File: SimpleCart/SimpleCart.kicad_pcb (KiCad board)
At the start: 2 copper layers, 90 x 56.8 mm, 9 parts, among them J1 CommanderX16Expansion Alt, U1 SST39SF040, U2 74HCT00, U3 74HCT138

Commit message: BOM, fully routed
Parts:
- C1, C2, C3: value C -> 100nF; footprint Capacitor_THT:C_Disc_D5.0mm_W2.5mm_P5.00mm -> Capacitor_THT:C_Axial_L3.8mm_D2.6mm_P7.50mm_Horizontal
- JP1: value Jumper_2_Bridged -> WRITE EN
- U1: value SST39SF040 -> SST39SF040 (ROM)
- moved C1 50.8 mm to (134.0, 115.5), turned to 90 degrees
- moved U1 28.8 mm to (129.1, 121.2), turned to 90 degrees
- moved U3 27.8 mm to (74.0, 121.5)
- moved JP1 26.5 mm to (108.2, 102.7), turned to 0 degrees
- moved C3 24.9 mm to (62.5, 109.9)
- moved U2 18.6 mm to (66.5, 102.2), turned to -90 degrees
- moved C2 12.7 mm to (77.7, 113.4), turned to -90 degrees
- moved R1 12.0 mm to (116.2, 102.7), turned to 0 degrees
- moved J1 0.60 mm to (93.0, 130.8)
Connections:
- net Net-(J1-A0) renamed A0
- net Net-(J1-A1) renamed A1
- net Net-(J1-A10) renamed A10
- net Net-(J1-A11) renamed A11
- net Net-(J1-A12) renamed A12
- net Net-(J1-A13) renamed A13
- net Net-(J1-A2) renamed A2
- net Net-(J1-A3) renamed A3
- net Net-(J1-A4) renamed A4
- net Net-(J1-A5) renamed A5
- net Net-(J1-A6) renamed A6
- net Net-(J1-A7) renamed A7
- net Net-(J1-A8) renamed A8
- net Net-(J1-A9) renamed A9
- net Net-(J1-D0) renamed D0
- net Net-(J1-D1) renamed D1
- net Net-(J1-D2) renamed D2
- net Net-(J1-D3) renamed D3
- net Net-(J1-D4) renamed D4
- net Net-(J1-D5) renamed D5
- net Net-(J1-D6) renamed D6
- net Net-(J1-D7) renamed D7
- net Net-(J1-ROMB0) renamed ROMB0
- net Net-(J1-ROMB1) renamed ROMB1
- net Net-(J1-ROMB2) renamed ROMB2
- net Net-(J1-ROMB3) renamed ROMB3
- net Net-(J1-ROMB4) renamed ROMB4
- U3 pad 14: unconnected-(U3-~{Y1}-Pad14) -> !RAMBEN
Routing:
- net +5V: track 0.00 -> 99.0 mm
- net GND: track 0.00 -> 96.6 mm
- net ROMB0: track 0.00 -> 73.8 mm, vias 0 -> 1
- net Net-(J1-A14): track 0.00 -> 67.6 mm, vias 0 -> 3
- net ROMB3: track 0.00 -> 65.9 mm, vias 0 -> 1
- net ROMB1: track 0.00 -> 64.6 mm
- net ROMB2: track 0.00 -> 64.4 mm
- net ROMB4: track 0.00 -> 63.7 mm, vias 0 -> 2
- net Net-(J1-A15): track 0.00 -> 60.2 mm, vias 0 -> 3
- net !ROMBEN: track 0.00 -> 41.7 mm
- net A10: track 0.00 -> 39.0 mm, vias 0 -> 1
- net Net-(J1-RWB): track 0.00 -> 38.4 mm, vias 0 -> 2
- net A11: track 0.00 -> 37.9 mm
- net Net-(J1-PHI2): track 0.00 -> 32.2 mm, vias 0 -> 2
- net !MEMWE: track 0.00 -> 30.9 mm
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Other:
- board text added: "<-- Rear of X16"
- board text added: "Cartridge PCB For the Commander X16 ONLY! This will very likely not work in other systems. Do not attempt to use in a Famicom or NES!"
- board text added: "Design By: Tim Sodersrtom"
- board text added: "Rear of X16 --->"
- board text added: "This side faces down"
- board text added: "This side faces up"

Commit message: Polish and a readme explaining WTF
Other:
- board text added: "Design By: Tim Soderstrom"
- board text removed: "Design By: Tim Sodersrtom"

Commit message: More tweaks
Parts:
- JP1: value WRITE EN -> WRITE ENABLE
- R1: value R -> 4.7k
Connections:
- U1 pad 22: !ROMBEN -> !CHIP1EN
- U3 pad 14: !RAMBEN -> !CHIP1EN
- U3 pad 15: !ROMBEN -> unconnected-(U3-~{Y0}-Pad15)
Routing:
- net !ROMBEN: track 41.7 -> 0.00 mm
- net (no net): track 0.00 -> 41.7 mm
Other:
- board text added: "+12V"
- board text added: "+5V"
- board text added: "-12V"
- board text added: "5V"
- board text added: "A11"
- board text added: "AUDIO L"
- board text added: "Back of cartridge (not label side)"
- board text added: "Cartridge PCB For the Commander X16 ONLY! Do not attempt to use in any other sytem (including NES/Famicom)"
- board text added: "Front of cartridge, label side"
- board text added: "GND"
- board text added: "ROMB7"
- board text added: "SCL"
- board text removed: "<-- Rear of X16"
- board text removed: "Cartridge PCB For the Commander X16 ONLY! This will very likely not work in other systems. Do not attempt to use in a Famicom or NES!"
- board text removed: "Rear of X16 --->"
- board text removed: "This side faces down"
- board text removed: "This side faces up"
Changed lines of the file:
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@@
 	(net 56 "D0")
 	(net 57 "!MEMWE")
-	(net 58 "!ROMBEN")
+	(net 58 "!CHIP1EN")
 	(net 59 "!MEMOE")
 	(net 60 "!ROMEN")
@@
 	(net 63 "unconnected-(U3-~{Y2}-Pad13)")
 	(net 64 "unconnected-(U3-~{Y7}-Pad7)")
-	(net 65 "!RAMBEN")
+	(net 65 "unconnected-(U3-~{Y0}-Pad15)")
 	(net 66 "unconnected-(U3-~{Y5}-Pad10)")
 	(net 67 "unconnected-(U3-~{Y3}-Pad12)")
@@
 			(layers "*.Cu" "*.Mask")
 			(remove_unused_layers no)
-			(net 58 "!ROMBEN")
+			(net 58 "!CHIP1EN")
 			(pinfunction "CE")
 			(pintype "input")
@@
 			)
 		)
-		(property "Value" "WRITE EN"
-			(at -5.05 0 0)
+		(property "Value" "WRITE ENABLE"
+			(at -6.75 0 0)
 			(layer "B.SilkS")
 			(effects
@@
 			(layers "*.Cu" "*.Mask")
 			(remove_unused_layers no)
-			(net 65 "!RAMBEN")
+			(net 58 "!CHIP1EN")
 			(pinfunction "~{Y1}")
 			(pintype "output")
@@
 			(layers "*.Cu" "*.Mask")
 			(remove_unused_layers no)
-			(net 58 "!ROMBEN")
+			(net 65 "unconnected-(U3-~{Y0}-Pad15)")
 			(pinfunction "~{Y0}")
 			(pintype "output")
@@
 			)
 		)
-		(property "Value" "R"
+		(property "Value" "4.7k"
 			(at 2.54 -1.92 0)
 			(layer "B.Fab")
@@
 		(layer "Edge.Cuts")
 	)
-	(gr_text "This side faces up"
-		(at 130.1 99 0)
+	(gr_text "+12V"
+		(at 56.7 123.9 90)
 		(layer "B.SilkS")
 		(effects
 			(font
-				(size 1 1)
+				(size 0.75 0.75)
+				(thickness 0.1)
+			)
+			(justify left bottom mirror)
+		)
+	)
+	(gr_text "SCL"
+		(at 125.3 124.6 90)
+		(layer "B.SilkS")
+		(effects
+			(font
+				(size 0.75 0.75)
+				(thickness 0.1)
+			)
+			(justify left bottom mirror)
+		)
+	)
+	(gr_text "GND"
+		(at 61.7 124.6 90)
+		(layer "B.SilkS")
+		(effects
+			(font
+				(size 0.75 0.75)
+				(thickness 0.1)
+			)
+			(justify left bottom mirror)
+		)
+	)
+	(gr_text "ROMB7"
+		(at 64.4 123.2 90)
+		(layer "B.SilkS")
+		(effects
+			(font
+				(size 0.75 0.75)
+				(thickness 0.1)
+			)
+			(justify left bottom mirror)
+		)
+	)
+	(gr_text "-12V"
+		(at 130.4 123.8 90)
+		(layer "B.SilkS")
+		(effects
+			(font
+				(size 0.75 0.75)
+				(thickness 0.1)
+			)
+			(justify left bottom mirror)
+		)
+	)
+	(gr_text "+5V"
+		(at 59.2 124.6 90)
+		(layer "B.SilkS")
+		(effects
+			(font
+				(size 0.75 0.75)
 				(thickness 0.1)
 			)
@@
 		)
 	)
-	(gr_text "Rear of X16 --->"
-		(at 69.2 98.3 0)
+	(gr_text "Front of cartridge, label side"
+		(at 129.7 98.6 0)
 		(layer "B.SilkS")
 		(effects
@@
 		)
 	)
-	(gr_text "Cartridge PCB For the Commander X16 ONLY!\nThis will very likely not work in other systems.\nDo not attempt to use in a Famicom or NES!"
-		(at 93.3 101 0)
+	(gr_text "GND\n"
+		(at 127.8 124.6 90)
+		(layer "B.SilkS")
+		(effects
+			(font
+				(size 0.75 0.75)
+				(thickness 0.1)
+			)
+			(justify left bottom mirror)
+		)
+	)
+	(gr_text "+12V"
+		(at 129.3 123.9 270)
 		(layer "F.SilkS")
 		(effects
 			(font
-				(size 1 1)
+				(size 0.75 0.75)
+				(thickness 0.1)
+			)
+			(justify left bottom)
+		)
+	)
+	(gr_text "GND"
+		(at 58.3 124.7 270)
+		(layer "F.SilkS")
+		(effects
+			(font
+				(size 0.75 0.75)
 				(thickness 0.1)
 			)
@@
 		)
 	)
-	(gr_text "<-- Rear of X16"
-		(at 55.3 98.3 0)
+	(gr_text "AUDIO L"
+		(at 60.8 122.6 270)
+		(layer "F.SilkS")
+		(effects
+			(font
+				(size 0.75 0.75)
+				(thickness 0.1)
+			)
+			(justify left bottom)
+		)
+	)
+	(gr_text "Cartridge PCB For the Commander X16 ONLY!\nDo not attempt to use in any other sytem\n(including NES/Famicom)"
+		(at 93 101.1 0)
 		(layer "F.SilkS")
 		(effects
@@
 		)
 	)
-	(gr_text "This side faces down"
-		(at 89.1 125.3 0)
+	(gr_text "5V"
+		(at 126.8 125.5 270)
+		(layer "F.SilkS")
+		(effects
+			(font
+				(size 0.75 0.75)
+				(thickness 0.1)
+			)
+			(justify left bottom)
+		)
+	)
+	(gr_text "Back of cartridge (not label side)"
+		(at 57.9 98 0)
 		(layer "F.SilkS")
 		(effects
@@
 		)
 	)
+	(gr_text "-12V"
+		(at 55.9 123.8 270)
+		(layer "F.SilkS")
+		(effects
+			(font
+				(size 0.75 0.75)
+				(thickness 0.1)
+			)
+			(justify left bottom)
+		)
+	)
+	(gr_text "GND"
+		(at 124.3 124.6 270)
+		(layer "F.SilkS")
+		(effects
+			(font
+				(size 0.75 0.75)
+				(thickness 0.1)
+			)
+			(justify left bottom)
+		)
+	)
+	(gr_text "A11"
+		(at 121.9 124.6 270)
+		(layer "F.SilkS")
+		(effects
+			(font
+				(size 0.75 0.75)
+				(thickness 0.1)
+			)
+			(justify left bottom)
+		)
+	)
 	(gr_text "Design By: Tim Soderstrom"
-		(at 57.1 105.4 0)
+		(at 58.3 105.2 0)
 		(layer "F.SilkS")
 		(effects
@@
 	)
 	(segment
+		(start 78.75 103.75)
+		(end 79.609925 103.75)
+		(width 0.1)
+		(layer "B.Cu")
+		(net 0)
+	)
+	(segment
+		(start 72.8 109.7)
+		(end 78.75 103.75)
+		(width 0.1)
+		(layer "B.Cu")
+		(net 0)
+	)
+	(segment
+		(start 79.609925 103.75)
+		(end 80.225 103.134925)
+		(width 0.1)
+		(layer "B.Cu")
+		(net 0)
+	)
+	(segment
+		(start 101.075 103.425)
+		(end 103.65 106)
+		(width 0.1)
+		(layer "B.Cu")
+		(net 0)
+	)
+	(segment
+		(start 80.225 102.190075)
+		(end 81.315075 101.1)
+		(width 0.1)
+		(layer "B.Cu")
+		(net 0)
+	)
+	(segment
+		(start 83.9 101.1)
+		(end 86 103.2)
+		(width 0.1)
+		(layer "B.Cu")
+		(net 0)
+	)
+	(segment
+		(start 100.85 103.2)
+		(end 101.075 103.425)
+		(width 0.1)
+		(layer "B.Cu")
+		(net 0)
+	)
+	(segment
+		(start 81.315075 101.1)
+		(end 83.9 101.1)
+		(width 0.1)
+		(layer "B.Cu")
+		(net 0)
+	)
+	(segment
+		(start 86 103.2)
+		(end 100.85 103.2)
+		(width 0.1)
+		(layer "B.Cu")
+		(net 0)
+	)
+	(segment
+		(start 72.8 111.3)
+		(end 72.8 109.7)
+		(width 0.1)
+		(layer "B.Cu")
+		(net 0)
+	)
+	(segment
+		(start 80.225 103.134925)
+		(end 80.225 102.190075)
+		(width 0.1)
+		(layer "B.Cu")
+		(net 0)
+	)
+	(segment
+		(start 71.46 113.88)
+		(end 71.46 112.64)
+		(width 0.1)
+		(layer "B.Cu")
+		(net 0)
+	)
+	(segment
+		(start 71.46 112.64)
+		(end 72.8 111.3)
+		(width 0.1)
+		(layer "B.Cu")
+		(net 0)
+	)
+	(segment
 		(start 93.69 123.58)
 		(end 96.03 121.24)
@@
 	)
 	(segment
-		(start 78.75 103.75)
-		(end 79.609925 103.75)
-		(width 0.1)
-		(layer "B.Cu")
-		(net 58)
-	)
-	(segment
-		(start 72.8 109.7)
-		(end 78.75 103.75)
-		(width 0.1)
-		(layer "B.Cu")
-		(net 58)
-	)
-	(segment
-		(start 79.609925 103.75)
-		(end 80.225 103.134925)
-		(width 0.1)
-		(layer "B.Cu")
-		(net 58)
-	)
-	(segment
-		(start 101.075 103.425)
-		(end 103.65 106)
-		(width 0.1)
-		(layer "B.Cu")
-		(net 58)
-	)
-	(segment
-		(start 80.225 102.190075)
-		(end 81.315075 101.1)
-		(width 0.1)
-		(layer "B.Cu")
-		(net 58)
-	)
-	(segment
-		(start 83.9 101.1)
-		(end 86 103.2)
-		(width 0.1)
-		(layer "B.Cu")
-		(net 58)
-	)
-	(segment
-		(start 100.85 103.2)
-		(end 101.075 103.425)
-		(width 0.1)
-		(layer "B.Cu")
-		(net 58)
-	)
-	(segment
-		(start 81.315075 101.1)
-		(end 83.9 101.1)
-		(width 0.1)
-		(layer "B.Cu")
-		(net 58)
-	)
-	(segment
-		(start 86 103.2)
-		(end 100.85 103.2)
-		(width 0.1)
-		(layer "B.Cu")
-		(net 58)
-	)
-	(segment
-		(start 72.8 111.3)
-		(end 72.8 109.7)
-		(width 0.1)
-		(layer "B.Cu")
-		(net 58)
-	)
-	(segment
-		(start 80.225 103.134925)
-		(end 80.225 102.190075)
-		(width 0.1)
-		(layer "B.Cu")
-		(net 58)
-	)
-	(segment
-		(start 71.46 113.88)
-		(end 71.46 112.64)
-		(width 0.1)
-		(layer "B.Cu")
-		(net 58)
-	)
-	(segment
-		(start 71.46 112.64)
-		(end 72.8 111.3)
-		(width 0.1)
-		(layer "B.Cu")
-		(net 58)
-	)
-	(segment

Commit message: Version #
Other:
- board text added: "X16 SimpleCart v0.00"
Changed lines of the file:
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@@
+		)
+	)
+	(gr_text "X16 SimpleCart v0.00"
+		(at 58.5 98.1 0)
+		(layer "F.SilkS")
+		(effects
+			(font
+				(size 1 1)
+				(thickness 0.1)
+			)
+			(justify left bottom)
 		)
 	)
@@
 	)
 	(gr_text "Back of cartridge (not label side)"
-		(at 57.9 98 0)
+		(at 58.2 108 0)
 		(layer "F.SilkS")
 		(effects

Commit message: Safe commit
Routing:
- net !CHIP1EN: track 0.00 -> 44.4 mm
- net (no net): track 41.7 -> 0.00 mm
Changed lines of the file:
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@@
-	)
-	(segment
-		(start 78.75 103.75)
-		(end 79.609925 103.75)
-		(width 0.1)
-		(layer "B.Cu")
-		(net 0)
-	)
-	(segment
-		(start 72.8 109.7)
-		(end 78.75 103.75)
-		(width 0.1)
-		(layer "B.Cu")
-		(net 0)
-	)
-	(segment
-		(start 79.609925 103.75)
-		(end 80.225 103.134925)
-		(width 0.1)
-		(layer "B.Cu")
-		(net 0)
-	)
-	(segment
-		(start 101.075 103.425)
-		(end 103.65 106)
-		(width 0.1)
-		(layer "B.Cu")
-		(net 0)
-	)
-	(segment
-		(start 80.225 102.190075)
-		(end 81.315075 101.1)
-		(width 0.1)
-		(layer "B.Cu")
-		(net 0)
-	)
-	(segment
-		(start 83.9 101.1)
-		(end 86 103.2)
-		(width 0.1)
-		(layer "B.Cu")
-		(net 0)
-	)
-	(segment
-		(start 100.85 103.2)
-		(end 101.075 103.425)
-		(width 0.1)
-		(layer "B.Cu")
-		(net 0)
-	)
-	(segment
-		(start 81.315075 101.1)
-		(end 83.9 101.1)
-		(width 0.1)
-		(layer "B.Cu")
-		(net 0)
-	)
-	(segment
-		(start 86 103.2)
-		(end 100.85 103.2)
-		(width 0.1)
-		(layer "B.Cu")
-		(net 0)
-	)
-	(segment
-		(start 72.8 111.3)
-		(end 72.8 109.7)
-		(width 0.1)
-		(layer "B.Cu")
-		(net 0)
-	)
-	(segment
-		(start 80.225 103.134925)
-		(end 80.225 102.190075)
-		(width 0.1)
-		(layer "B.Cu")
-		(net 0)
-	)
-	(segment
-		(start 71.46 113.88)
-		(end 71.46 112.64)
-		(width 0.1)
-		(layer "B.Cu")
-		(net 0)
-	)
-	(segment
-		(start 71.46 112.64)
-		(end 72.8 111.3)
-		(width 0.1)
-		(layer "B.Cu")
-		(net 0)
 	)
 	(segment
@@
 	)
 	(segment
+		(start 103.65 106)
+		(end 100.85 103.2)
+		(width 0.1)
+		(layer "B.Cu")
+		(net 58)
+	)
+	(segment
+		(start 80.225 103.134925)
+		(end 78.659925 104.7)
+		(width 0.1)
+		(layer "B.Cu")
+		(net 58)
+	)
+	(segment
+		(start 78.659925 104.7)
+		(end 75.1 104.7)
+		(width 0.1)
+		(layer "B.Cu")
+		(net 58)
+	)
+	(segment
+		(start 75.1 104.7)
+		(end 70.3 109.5)
+		(width 0.1)
+		(layer "B.Cu")
+		(net 58)
+	)
+	(segment
+		(start 86 103.2)
+		(end 83.9 101.1)
+		(width 0.1)
+		(layer "B.Cu")
+		(net 58)
+	)
+	(segment
+		(start 83.9 101.1)
+		(end 81.315075 101.1)
+		(width 0.1)
+		(layer "B.Cu")
+		(net 58)
+	)
+	(segment
+		(start 70.3 109.5)
+		(end 70.3 112.5)
+		(width 0.1)
+		(layer "B.Cu")
+		(net 58)
+	)
+	(segment
+		(start 100.85 103.2)
+		(end 86 103.2)
+		(width 0.1)
+		(layer "B.Cu")
+		(net 58)
+	)
+	(segment
+		(start 70.3 112.5)
+		(end 68.92 113.88)
+		(width 0.1)
+		(layer "B.Cu")
+		(net 58)
+	)
+	(segment
+		(start 80.225 102.190075)
+		(end 80.225 103.134925)
+		(width 0.1)
+		(layer "B.Cu")
+		(net 58)
+	)
+	(segment
+		(start 81.315075 101.1)
+		(end 80.225 102.190075)
+		(width 0.1)
+		(layer "B.Cu")
+		(net 58)
+	)
+	(segment

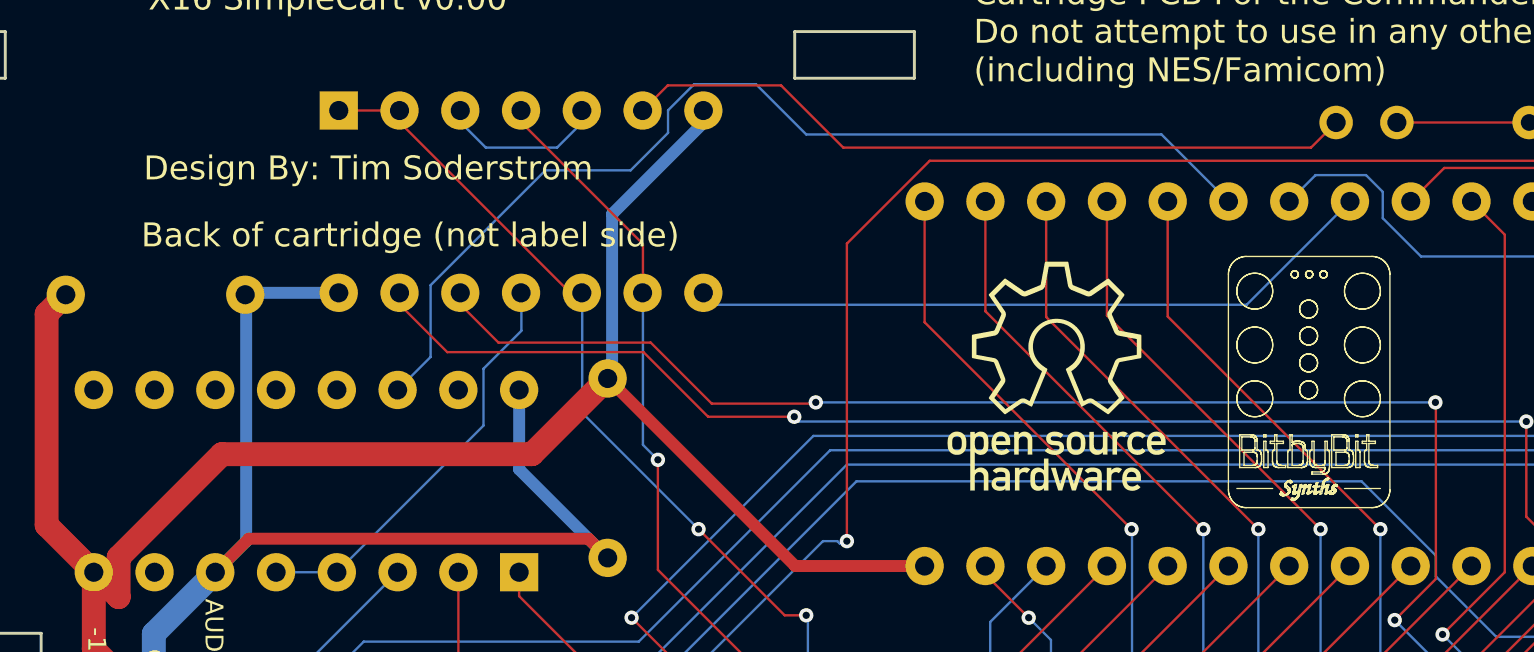
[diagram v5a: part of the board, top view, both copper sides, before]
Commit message: Removed references to me and the synth store
Since the project now has other contributors I didn't feel right
comandeering the silkscreen with my logo
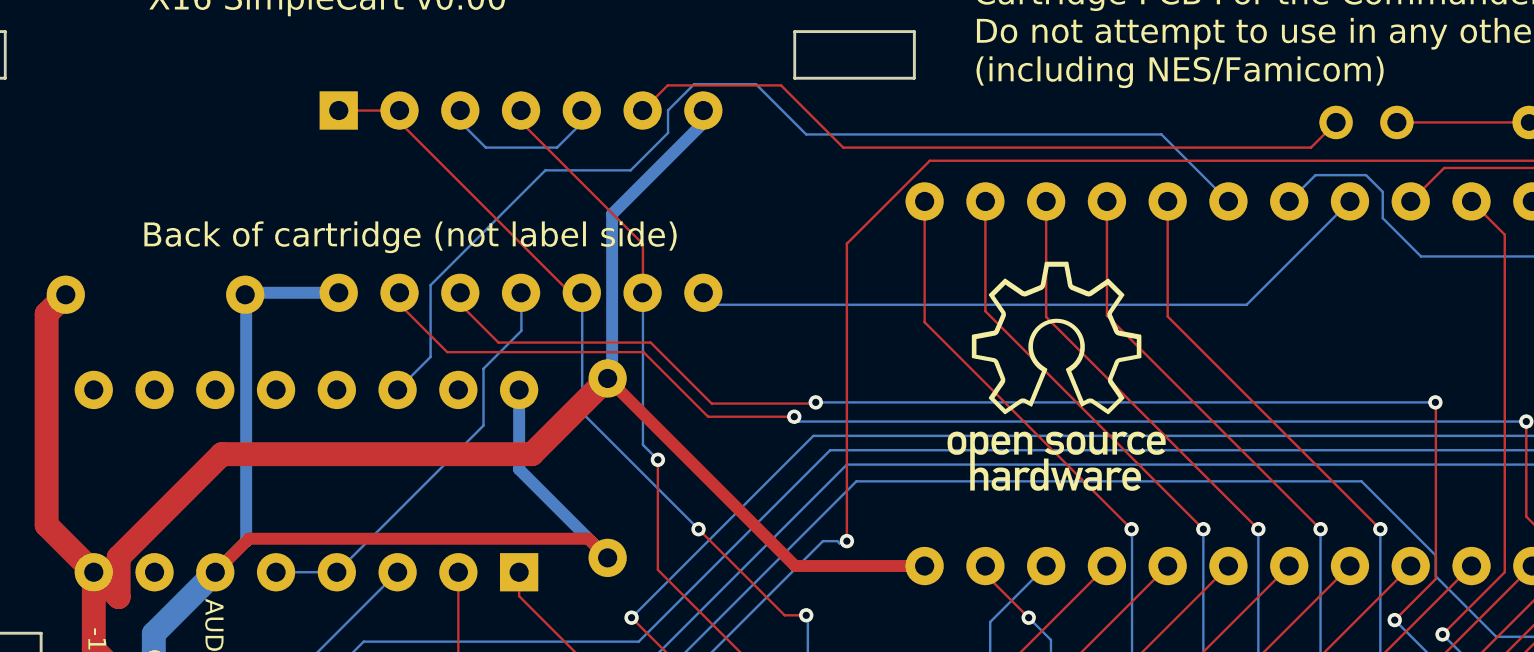
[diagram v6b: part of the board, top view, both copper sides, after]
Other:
- board text removed: "Design By: Tim Soderstrom"
